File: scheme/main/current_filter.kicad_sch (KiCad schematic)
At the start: 8 parts, among them U6 RS8551

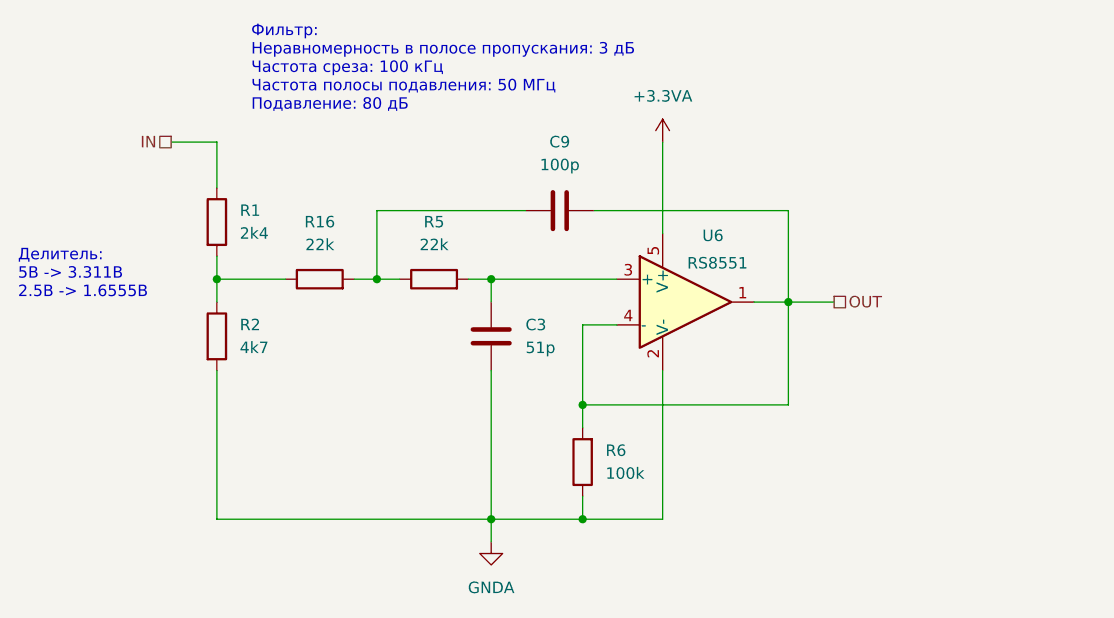
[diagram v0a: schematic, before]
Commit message: bootstrap schematic & itrip on separated list
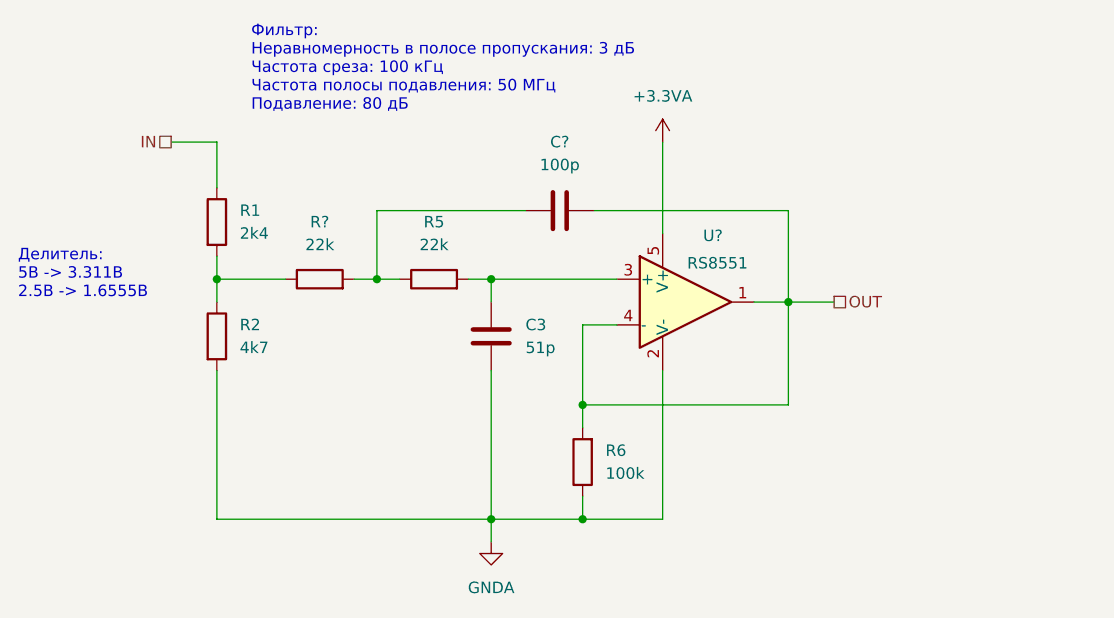
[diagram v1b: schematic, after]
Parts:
- renumbered C9 to C?, R16 to R?, U6 to U?
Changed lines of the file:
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@@
 		(shape passive)
 		(at 132.08 68.58 0)
+		(fields_autoplaced yes)
 		(effects
 			(font
@@
 		(shape passive)
 		(at 58.42 50.8 180)
+		(fields_autoplaced yes)
 		(effects
 			(font
@@
 		(dnp no)
 		(fields_autoplaced yes)
-		(property "Reference" "R16"
+		(property "Reference" "R?"
 			(at 74.93 59.69 90)
 			(effects
@@
 		(on_board yes)
 		(dnp no)
-		(property "Reference" "U6"
+		(property "Reference" "U?"
 			(at 118.618 61.214 0)
 			(effects
@@
 		(dnp no)
 		(fields_autoplaced yes)
-		(property "Reference" "C9"
+		(property "Reference" "C?"
 			(at 101.6 50.8 90)
 			(effects
@@
 		(dnp no)
 		(fields_autoplaced yes)
-		(property "Reference" "#PWR12"
+		(property "Reference" "#PWR?"
 			(at 113.03 54.61 0)
 			(effects
@@
 		(dnp no)
 		(fields_autoplaced yes)
-		(property "Reference" "#PWR11"
+		(property "Reference" "#PWR?"
 			(at 93.98 101.6 0)
 			(effects

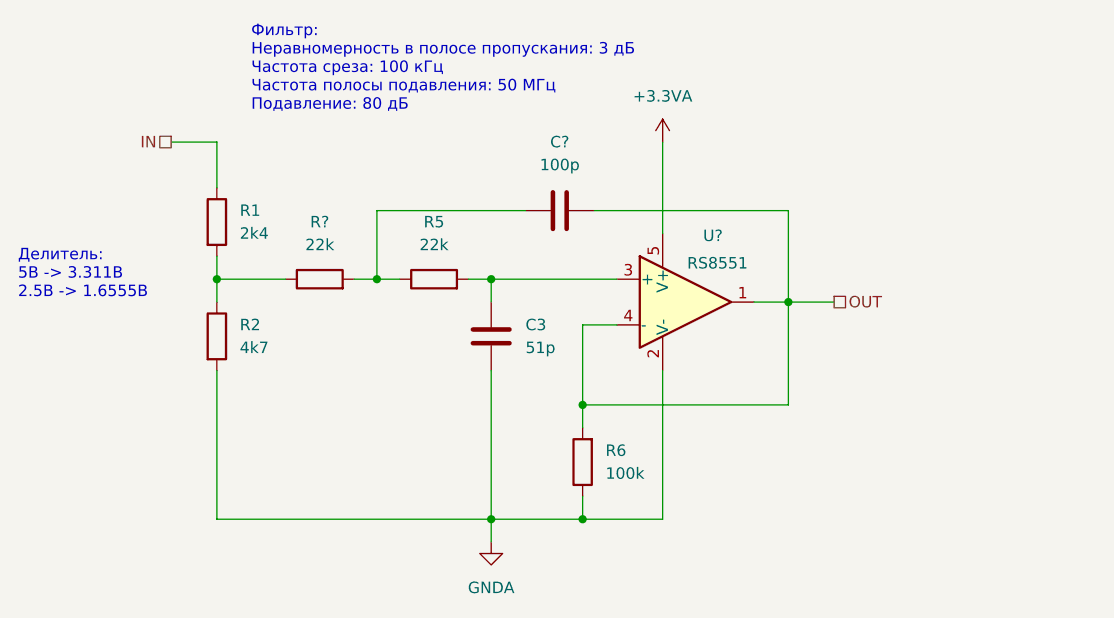
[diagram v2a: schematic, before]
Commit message: added decoupling capacitors
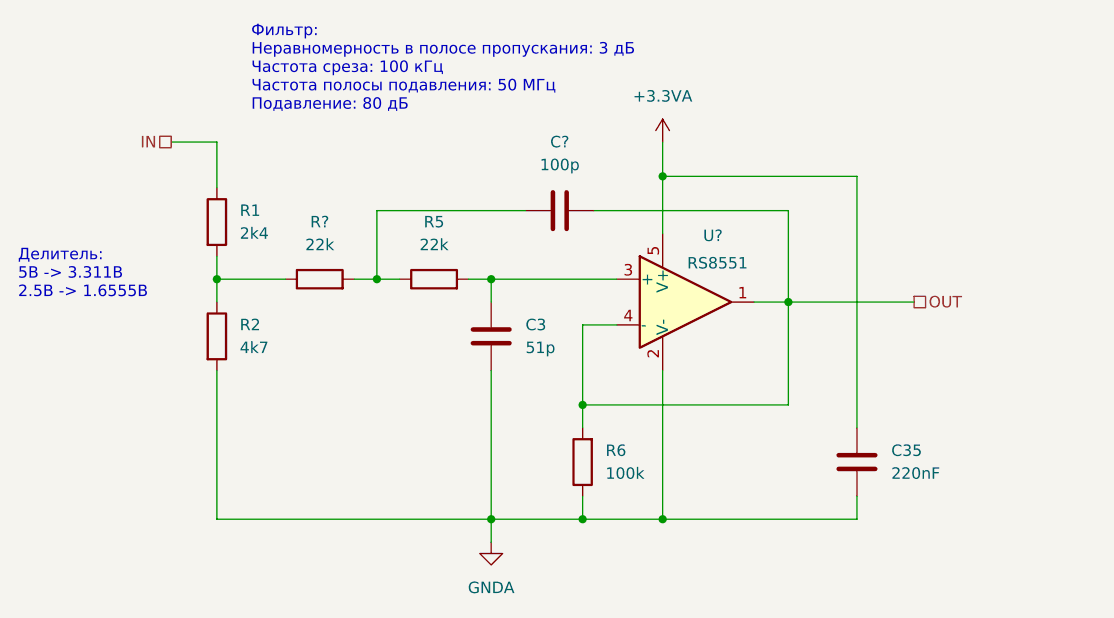
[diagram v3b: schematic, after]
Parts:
- added C35: 220nF, Capacitor_SMD:C_0805_2012Metric, symbol Device:C
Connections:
- net +3.3VA: now also C35.1
- net GNDA: now also C35.2
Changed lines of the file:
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@@
+	)
+	(junction
+		(at 113.03 92.71)
+		(diameter 0)
+		(color 0 0 0 0)
 	)
 	(junction
@@
 	)
 	(junction
+		(at 113.03 54.61)
+		(diameter 0)
+		(color 0 0 0 0)
+	)
+	(junction
 		(at 93.98 66.04)
 		(diameter 0)
@@
 	(wire
 		(pts
+			(xy 113.03 54.61) (xy 113.03 60.96)
+		)
+		(stroke
+			(width 0)
+			(type default)
+		)
+	)
+	(wire
+		(pts
 			(xy 104.14 92.71) (xy 113.03 92.71)
 		)
@@
 	(wire
 		(pts
-			(xy 127 68.58) (xy 132.08 68.58)
+			(xy 127 68.58) (xy 140.97 68.58)
 		)
 		(stroke
@@
 	(wire
 		(pts
-			(xy 113.03 50.8) (xy 113.03 60.96)
+			(xy 113.03 50.8) (xy 113.03 54.61)
 		)
 		(stroke
@@
 	(wire
 		(pts
+			(xy 134.62 90.17) (xy 134.62 92.71)
+		)
+		(stroke
+			(width 0)
+			(type default)
+		)
+	)
+	(wire
+		(pts
 			(xy 105.41 58.42) (xy 127 58.42)
 		)
@@
 	(wire
 		(pts
+			(xy 113.03 92.71) (xy 134.62 92.71)
+		)
+		(stroke
+			(width 0)
+			(type default)
+		)
+	)
+	(wire
+		(pts
 			(xy 81.28 58.42) (xy 81.28 66.04)
 		)
@@
 	(wire
 		(pts
+			(xy 134.62 54.61) (xy 113.03 54.61)
+		)
+		(stroke
+			(width 0)
+			(type default)
+		)
+	)
+	(wire
+		(pts
 			(xy 93.98 76.2) (xy 93.98 92.71)
 		)
@@
 		(pts
 			(xy 91.44 66.04) (xy 93.98 66.04)
+		)
+		(stroke
+			(width 0)
+			(type default)
+		)
+	)
+	(wire
+		(pts
+			(xy 134.62 82.55) (xy 134.62 54.61)
 		)
 		(stroke
@@
 	(hierarchical_label "OUT"
 		(shape passive)
-		(at 132.08 68.58 0)
+		(at 140.97 68.58 0)
 		(effects
 			(font
@@
 		)
 	)
+	(symbol
+		(lib_id "Device:C")
+		(at 134.62 86.36 0)
+		(unit 1)
+		(exclude_from_sim no)
+		(in_bom yes)
+		(on_board yes)
+		(dnp no)
+		(fields_autoplaced yes)
+		(property "Reference" "C35"
+			(at 138.43 85.0899 0)
+			(effects
+				(font
+					(size 1.27 1.27)
+				)
+				(justify left)
+			)
+		)
+		(property "Value" "220nF"
+			(at 138.43 87.6299 0)
+			(effects
+				(font
+					(size 1.27 1.27)
+				)
+				(justify left)
+			)
+		)
+		(property "Footprint" "Capacitor_SMD:C_0805_2012Metric"
+			(at 135.5852 90.17 0)
+			(effects
+				(font
+					(size 1.27 1.27)
+				)
+				(hide yes)
+			)
+		)
+		(property "Datasheet" "~"
+			(at 134.62 86.36 0)
+			(effects
+				(font
+					(size 1.27 1.27)
+				)
+				(hide yes)
+			)
+		)
+		(property "Description" "Unpolarized capacitor"
+			(at 134.62 86.36 0)
+			(effects
+				(font
+					(size 1.27 1.27)
+				)
+				(hide yes)
+			)
+		)
+		(pin "2"
+		)
+		(pin "1"
+		)
+		(instances
+			(project "main"
+				(path "/c11d1dbc-4db9-4712-8d1d-5f6f7086cded/4b1be1b1-dfa5-4b57-a4fe-e097b3b33d8a"
+					(reference "C35")
+					(unit 1)
+				)
+				(path "/c11d1dbc-4db9-4712-8d1d-5f6f7086cded/5abad072-255e-43b5-81ad-39000e042b96"
+					(reference "C37")
+					(unit 1)
+				)
+				(path "/c11d1dbc-4db9-4712-8d1d-5f6f7086cded/b143e45b-d52c-4c1e-956d-7828de21cc22"
+					(reference "C36")
+					(unit 1)
+				)
+			)
+		)
+	)

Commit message: control isolation schematic
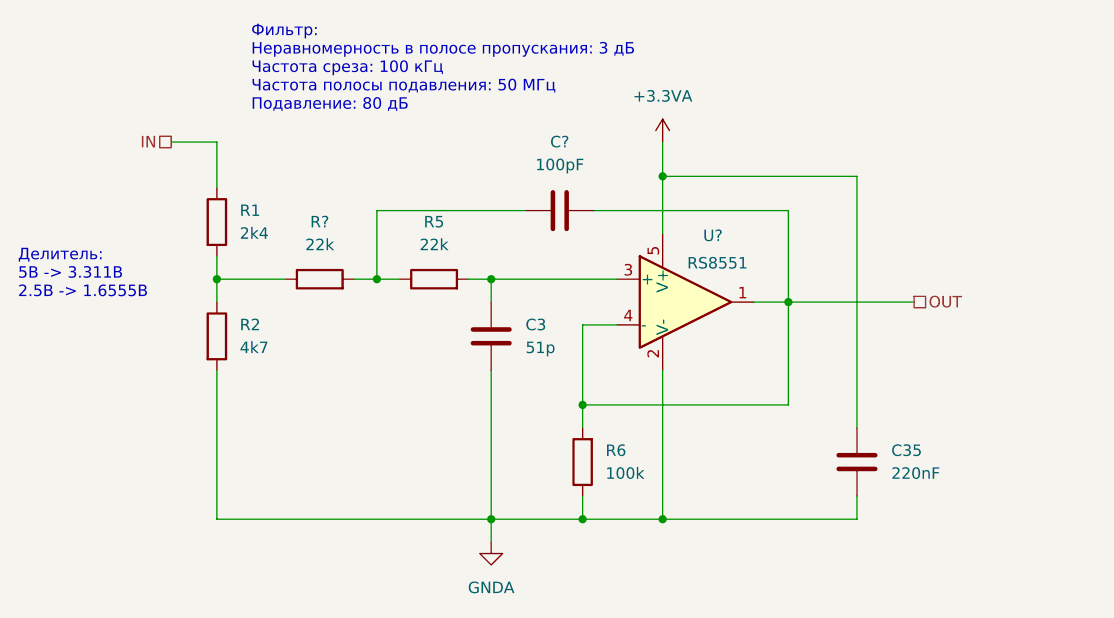
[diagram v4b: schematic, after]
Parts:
- C3: footprint Diode_SMD:D_0805_2012Metric -> Capacitor_SMD:C_0805_2012Metric
- C?: value 100p -> 100pF; footprint Diode_SMD:D_0805_2012Metric -> Capacitor_SMD:C_0805_2012Metric
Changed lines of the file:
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@@
 			)
 		)
-		(property "Footprint" "Diode_SMD:D_0805_2012Metric"
+		(property "Footprint" "Capacitor_SMD:C_0805_2012Metric"
 			(at 94.9452 76.2 0)
 			(effects
@@
 			)
 		)
-		(property "Value" "100p"
+		(property "Value" "100pF"
 			(at 101.6 53.34 90)
 			(effects
@@
 			)
 		)
-		(property "Footprint" "Diode_SMD:D_0805_2012Metric"
+		(property "Footprint" "Capacitor_SMD:C_0805_2012Metric"
 			(at 97.79 59.3852 0)
 			(effects

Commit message: boards schematic sheets & more
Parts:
- added R102: 22R, Resistor_SMD:R_0805_2012Metric, symbol Device:R
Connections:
- net OUT: now also R102.2; no longer C?.1, R6.2, U?.1, U?.4 (-)
- new net: C?.1, R102.1, R6.2, U?.1, U?.4 (-)
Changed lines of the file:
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@@
 	(wire
 		(pts
-			(xy 127 68.58) (xy 140.97 68.58)
+			(xy 127 68.58) (xy 139.7 68.58)
 		)
 		(stroke
@@
 		(pts
 			(xy 63.5 66.04) (xy 71.12 66.04)
+		)
+		(stroke
+			(width 0)
+			(type default)
+		)
+	)
+	(wire
+		(pts
+			(xy 147.32 68.58) (xy 154.94 68.58)
 		)
 		(stroke
@@
 	(hierarchical_label "OUT"
 		(shape passive)
-		(at 140.97 68.58 0)
+		(at 154.94 68.58 0)
 		(fields_autoplaced yes)
 		(effects
@@
 					(unit 1)
 				)
+			)
+		)
+	)
+	(symbol
+		(lib_id "Device:R")
+		(at 143.51 68.58 90)
+		(unit 1)
+		(exclude_from_sim no)
+		(in_bom yes)
+		(on_board yes)
+		(dnp no)
+		(fields_autoplaced yes)
+		(property "Reference" "R102"
+			(at 143.51 62.23 90)
+			(effects
+				(font
+					(size 1.27 1.27)
+				)
+			)
+		)
+		(property "Value" "22R"
+			(at 143.51 64.77 90)
+			(effects
+				(font
+					(size 1.27 1.27)
+				)
+			)
+		)
+		(property "Footprint" "Resistor_SMD:R_0805_2012Metric"
+			(at 143.51 70.358 90)
+			(effects
+				(font
+					(size 1.27 1.27)
+				)
+				(hide yes)
+			)
+		)
+		(property "Datasheet" "~"
+			(at 143.51 68.58 0)
+			(effects
+				(font
+					(size 1.27 1.27)
+				)
+				(hide yes)
+			)
+		)
+		(property "Description" "Resistor"
+			(at 143.51 68.58 0)
+			(effects
+				(font
+					(size 1.27 1.27)
+				)
+				(hide yes)
+			)
+		)
+		(pin "1"
+		)
+		(pin "2"
+		)
+		(instances
+			(project "main"
+				(path "/c11d1dbc-4db9-4712-8d1d-5f6f7086cded/4b1be1b1-dfa5-4b57-a4fe-e097b3b33d8a"
+					(reference "R102")
+					(unit 1)
+				)
+				(path "/c11d1dbc-4db9-4712-8d1d-5f6f7086cded/5abad072-255e-43b5-81ad-39000e042b96"
+					(reference "R104")
+					(unit 1)
+				)
+				(path "/c11d1dbc-4db9-4712-8d1d-5f6f7086cded/b143e45b-d52c-4c1e-956d-7828de21cc22"
+					(reference "R103")
+					(unit 1)
+				)
